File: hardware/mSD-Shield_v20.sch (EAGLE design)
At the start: 63 parts, among them IC1 74LVC244, IC2 DS1307, Q1 32kHz, Q1B 32kHz, U1 TS5204-3V3, X1 PASSER, X2 PASSER, X3 PASSER, X4 PASSER, X5 MICRO-SD

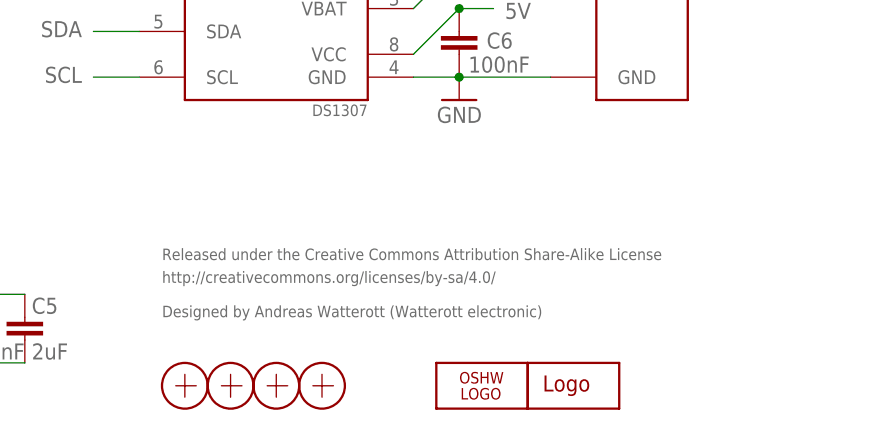
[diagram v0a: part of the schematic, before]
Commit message: updated schematics
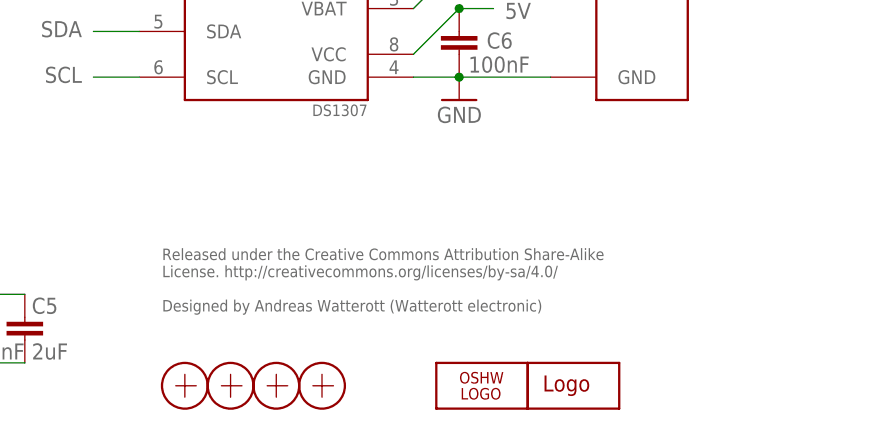
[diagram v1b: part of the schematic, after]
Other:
- note added: "Released under the Creative Commons Attribution Share-Alike License. http://creativecommons.org/licenses/by-sa/4.0/ Designed by Andreas Watterott (Watterott electronic)"
- note removed: "Designed by Andreas Watterott (Watterott electronic)"
- note removed: "Released under the Creative Commons Attribution Share-Alike License"
- note removed: "http://creativecommons.org/licenses/by-sa/4.0/"
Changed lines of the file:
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@@
 <?xml version="1.0" encoding="utf-8"?>
 <!DOCTYPE eagle SYSTEM "eagle.dtd">
-<eagle version="6.6.0">
+<eagle version="7.5.0">
 <drawing>
 <settings>
@@
 <layer number="51" name="tDocu" color="7" fill="1" visible="no" active="no"/>
 <layer number="52" name="bDocu" color="7" fill="1" visible="no" active="no"/>
-<layer number="53" name="tCopper" color="7" fill="11" visible="no" active="no"/>
-<layer number="54" name="bCopper" color="7" fill="1" visible="no" active="no"/>
-<layer number="56" name="wert" color="7" fill="1" visible="no" active="no"/>
 <layer number="91" name="Nets" color="2" fill="1" visible="yes" active="yes"/>
 <layer number="92" name="Busses" color="1" fill="1" visible="yes" active="yes"/>
@@
 <layer number="97" name="Info" color="7" fill="1" visible="yes" active="yes"/>
 <layer number="98" name="Guide" color="6" fill="1" visible="yes" active="yes"/>
-<layer number="100" name="Muster" color="7" fill="1" visible="no" active="no"/>
 <layer number="250" name="Descript" color="3" fill="1" visible="yes" active="yes"/>
-<layer number="251" name="SMDround" color="12" fill="11" visible="no" active="no"/>
 </layers>
 <schematic xreflabel="%F%N/%S.%C%R" xrefpart="/%S.%C%R">
@@
 <wire x1="88.265" y1="17.78" x2="90.297" y2="17.78" width="0.8128" layer="94"/>
 <wire x1="77.47" y1="80.01" x2="75.438" y2="80.01" width="0.8128" layer="94"/>
-<text x="162.56" y="21.59" size="1.27" layer="95">Released under the Creative Commons Attribution Share-Alike License</text>
-<text x="162.56" y="19.05" size="1.27" layer="95">http://creativecommons.org/licenses/by-sa/4.0/</text>
-<text x="162.56" y="15.24" size="1.27" layer="95">Designed by Andreas Watterott (Watterott electronic)</text>
+<text x="162.56" y="22.86" size="1.27" layer="95" align="top-left">Released under the Creative Commons Attribution Share-Alike
+License. http://creativecommons.org/licenses/by-sa/4.0/
+Designed by Andreas Watterott (Watterott electronic)</text>
 <text x="46.99" y="105.41" size="1.778" layer="95">(EthShield uses 2, 4, 10_SS)</text>
 <text x="30.48" y="76.2" size="1.27" layer="95" rot="R180">LCD_LED/GPIO</text>
@@
 </schematic>
 </drawing>
+<compatibility>
+<note version="6.3" minversion="6.2.2" severity="warning">
+Since Version 6.2.2 text objects can contain more than one line,
+which will not be processed correctly with this version.
+</note>
+</compatibility>
 </eagle>
